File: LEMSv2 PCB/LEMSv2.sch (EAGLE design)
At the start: 18 parts, among them J2 M05, J7 FEMALE 2x3, U1 SDMMC06132, U2 DS3231

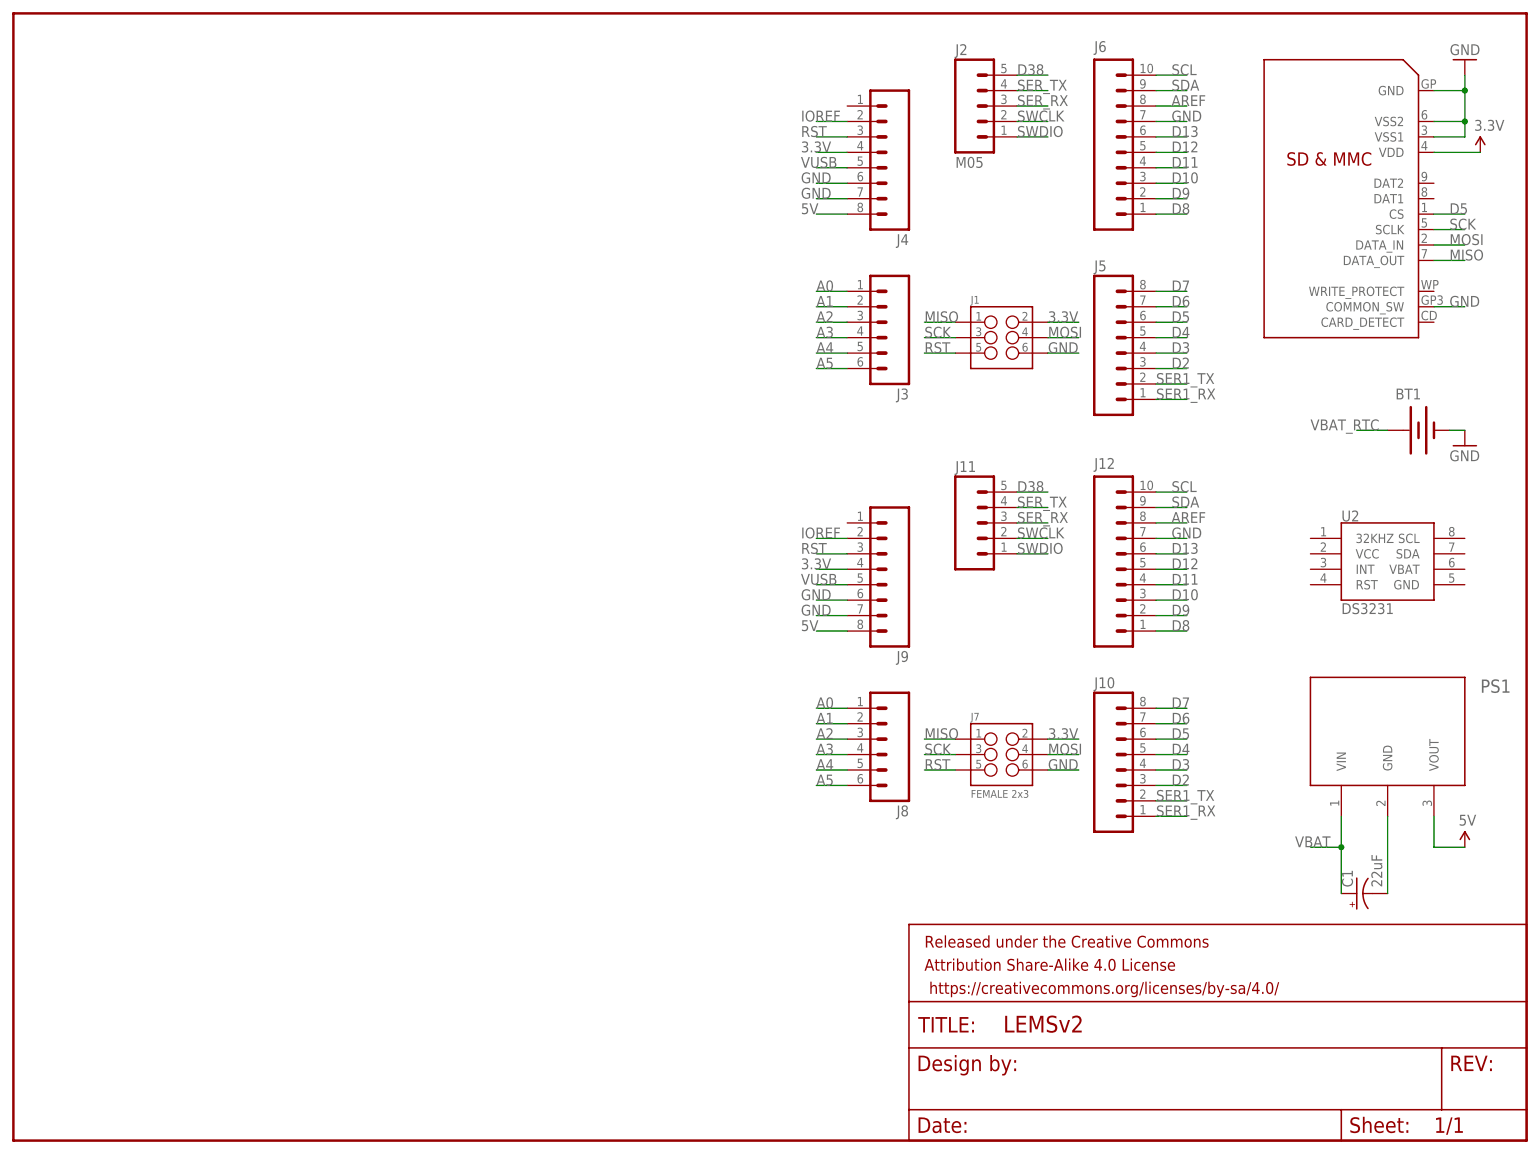
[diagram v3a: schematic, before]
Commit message: Added more parts to schematic
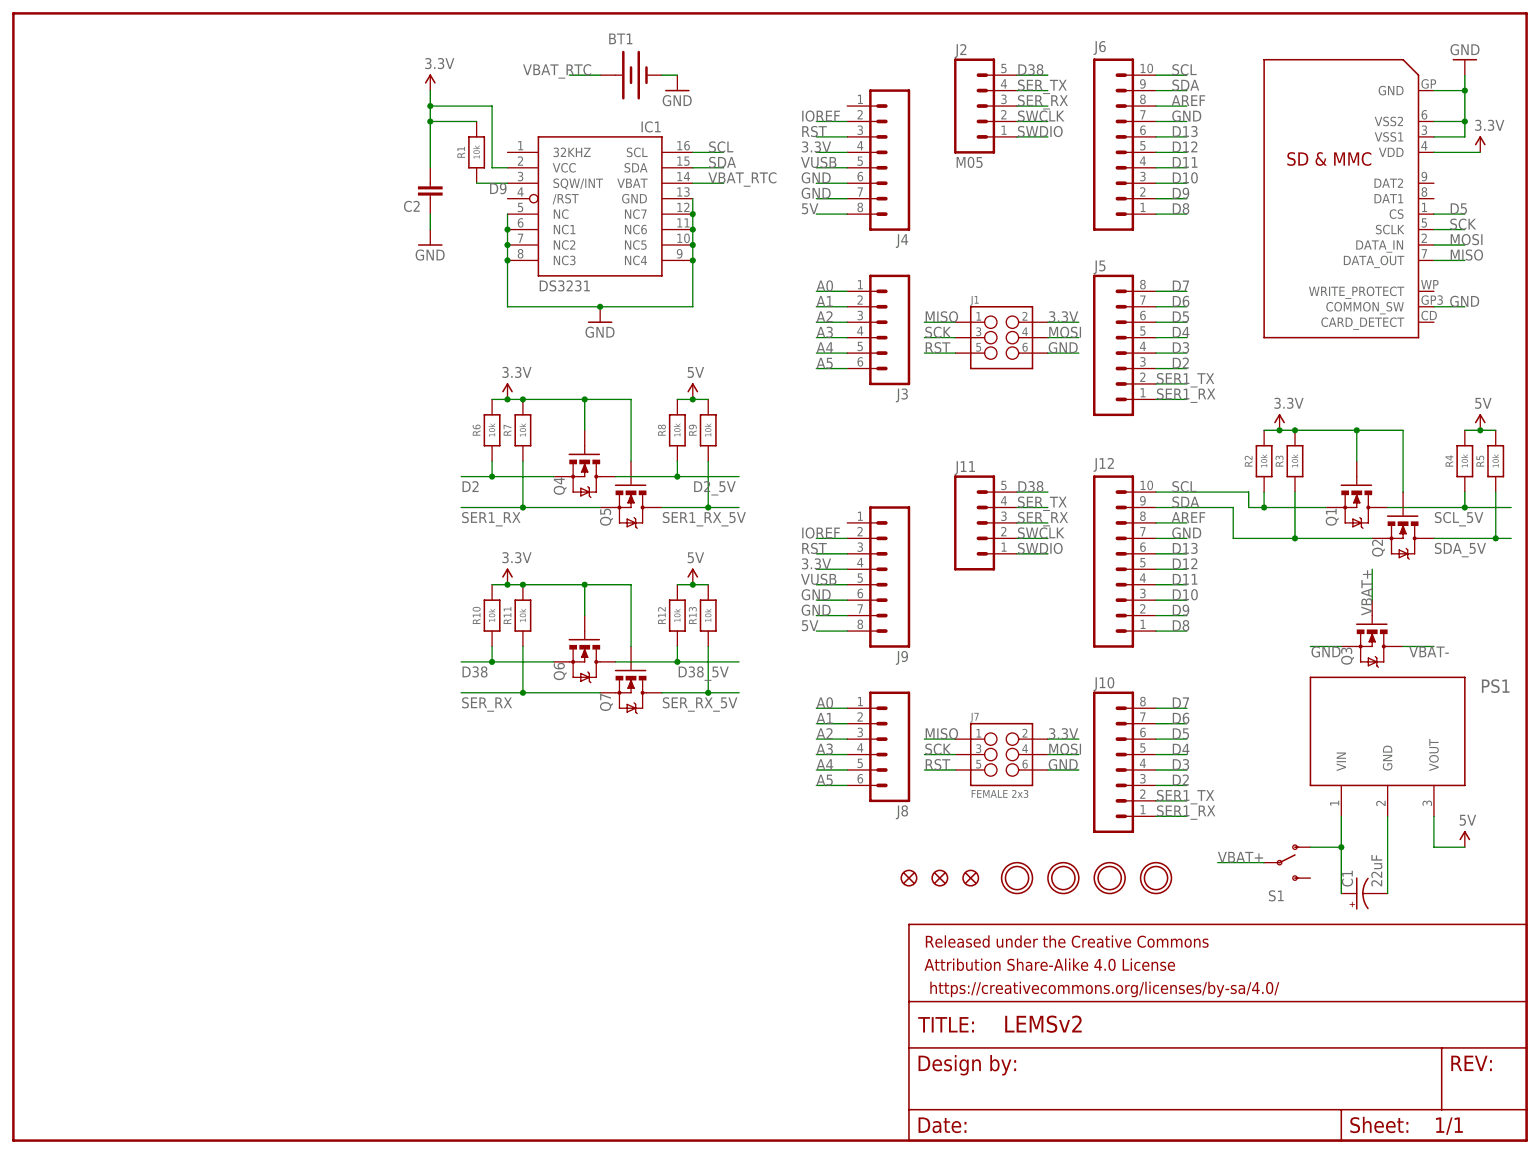
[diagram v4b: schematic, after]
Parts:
- removed U2: DS3231, LEMSv2:DS3231
- added C2: (no value), LEMSv2:CAP0805
- added FID1, FID2, FID3: FIDUCIAL"", LEMSv2:FIDUCIAL""
- added IC1: DS3231/SO, LEMSv2:DS3231/SO
- added Q1, Q2: 200mA/50V, SparkFun-DiscreteSemi:MOSFET-NCHANNELBSS138
- added Q3, Q4, Q5, Q6, Q7: 200mA/50V, LEMSv2:MOSFET-NCHANNELBSS138
- added R1, R10, R11, R12, R13, R2, R3, R4, R5, R6, R7, R8, R9: 10k, LEMSv2:RESISTOR_0805
- added S1: (no value), SparkFun-Electromechanical:SWITCH-SPDTPTH
- added U$1, U$2, U$3, U$4: MOUNTINGHOLE2.5, LEMSv2:MOUNTINGHOLE2.5
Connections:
- removed net VBAT: C1.+, PS1.VIN
- new net D2_5V: Q4.D, R8.1
- new net D38_5V: Q6.D, R12.1
- new net N$1: C1.+, PS1.VIN, S1.O
- new net SCL_5V: Q1.D, R4.1
- new net SDA_5V: Q2.D, R5.1
- new net SER1_RX_5V: Q5.D, R9.1
- new net SER_RX_5V: Q7.D, R13.1
- new net VBAT+: Q3.G, S1.P
- new net VBAT-: Q3.D
- net 3.3V: now also C2.2, IC1.VCC, Q1.G, Q2.G, Q4.G, Q5.G, Q6.G, Q7.G, R1.2, R10.2, R11.2, R2.2, R3.2, R6.2, R7.2
- net 5V: now also R12.2, R13.2, R4.2, R5.2, R8.2, R9.2
- net D2: now also Q4.S, R6.1
- net D38: now also Q6.S, R10.1
- net D9: now also IC1.SQW/INT, R1.1
- net GND: now also C2.1, IC1.GND, IC1.NC, IC1.NC1, IC1.NC2, IC1.NC3, IC1.NC4, IC1.NC5, IC1.NC6, IC1.NC7, Q3.S
- net SCL: now also IC1.SCL, Q1.S, R2.1
- net SDA: now also IC1.SDA, Q2.S, R3.1
- net SER1_RX: now also Q5.S, R7.1
- net SER_RX: now also Q7.S, R11.1
- net VBAT_RTC: now also IC1.VBAT
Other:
- moved on the sheet: BT1

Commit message: Added circuits to schematic
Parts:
- added C3: 0.1uF, LEMSv2:CAP0805
- added C4: 1uF, LEMSv2:CAP0805
- added C5, C6: (no value), LEMSv2:CAP0805
- added J13: (no value), LEMSv2:M03PTH
- added R14: (no value), adafruit:R-US_FLIPFLOP
- added U3: TLV2372, LEMSv2:TLV2372
- added U4: BMP280, LEMSv2:BMP280
- renumbered IC1 to U2
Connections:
- new net LIOUT: C4.2, R14.2, U3TLV2372-1.OUT
- new net LI_IN-: C4.1, R14.1, U3TLV2372-1.-IN
- new net N$2: J13.2, U3TLV2372-2.-IN
- new net N$3: J13.1, U3TLV2372-2.+IN
- new net N$4: J13.3, U3TLV2372-2.OUT
- net 3.3V: now also C5.1, C6.1, U4.CSB, U4.SDO, U4.VDD, U4.VDDIO
- net 5V: now also C3.1, U3TLV2372-PWRN.VCC
- net GND: now also C3.2, C5.2, C6.2, U3TLV2372-1.+IN, U3TLV2372-PWRN.GND, U4.GND@1, U4.GND@7
- net SCL: now also U4.SCK
- net SDA: now also U4.SDI

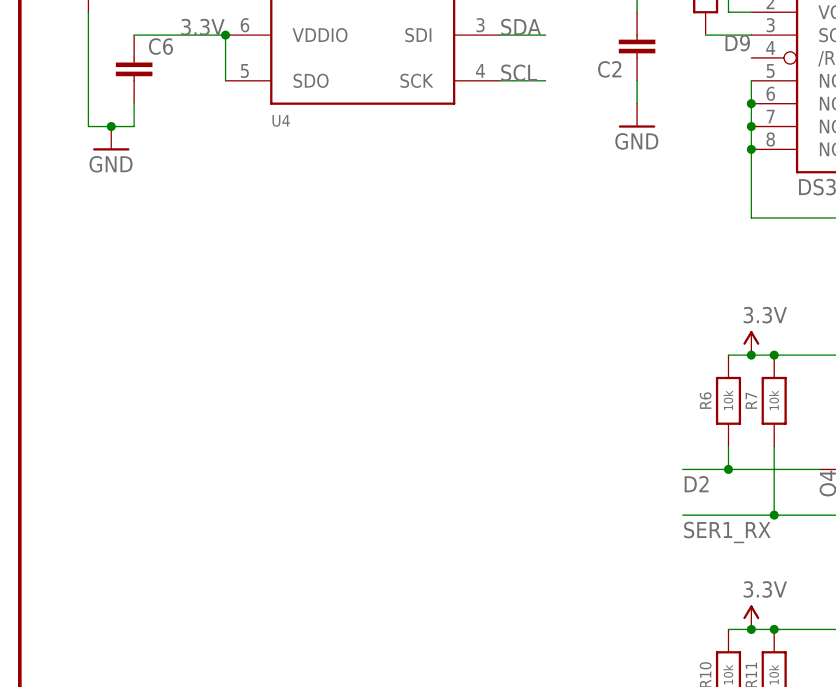
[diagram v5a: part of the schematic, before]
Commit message: Added LED circuit
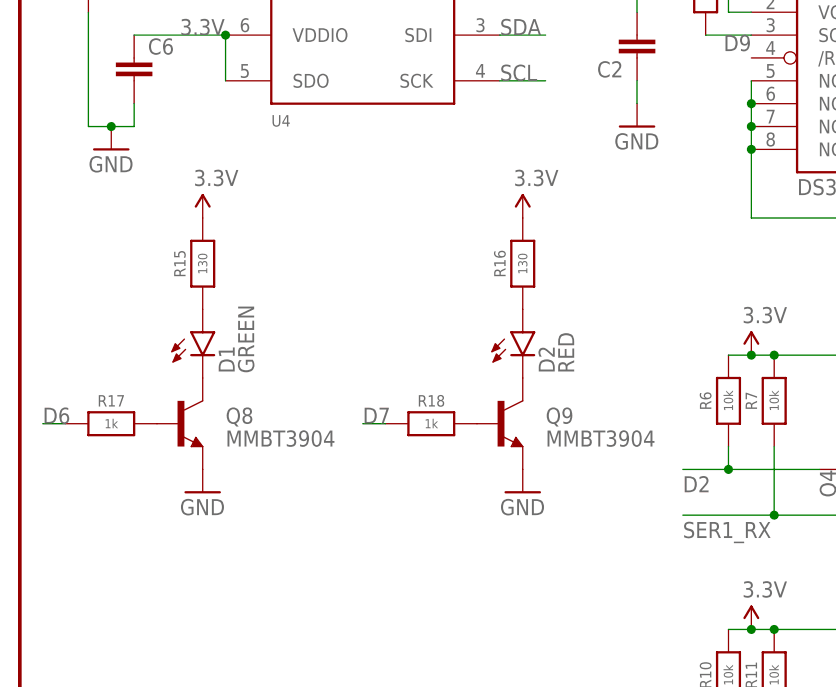
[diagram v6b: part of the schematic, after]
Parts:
- added D1: GREEN, LEMSv2:LED_GREEN
- added D2: RED, LEMSv2:LED_RED
- added Q8, Q9: MMBT3904, LEMSv2:MMBT3904
- added R15, R16: 130, LEMSv2:RESISTOR_0805
- added R17, R18: 1k, LEMSv2:RESISTOR_0805
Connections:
- new net N$10: D2.A, R16.1
- new net N$5: Q8.B, R17.2
- new net N$6: Q9.B, R18.2
- new net N$7: D1.C, Q8.C
- new net N$8: D2.C, Q9.C
- new net N$9: D1.A, R15.1
- net 3.3V: now also R15.2, R16.2
- net D6: now also R17.1
- net D7: now also R18.1
- net GND: now also Q8.E, Q9.E
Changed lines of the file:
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@@
 <part name="C6" library="LEMSv2" deviceset="CAP" device="0805"/>
 <part name="GND7" library="LEMSv2" deviceset="GND" device=""/>
+<part name="Q8" library="LEMSv2" deviceset="MMBT3904" device=""/>
+<part name="Q9" library="LEMSv2" deviceset="MMBT3904" device=""/>
+<part name="GND8" library="LEMSv2" deviceset="GND" device=""/>
+<part name="GND9" library="LEMSv2" deviceset="GND" device=""/>
+<part name="R15" library="LEMSv2" deviceset="RESISTOR" device="_0805" value="130"/>
+<part name="R16" library="LEMSv2" deviceset="RESISTOR" device="_0805" value="130"/>
+<part name="R17" library="LEMSv2" deviceset="RESISTOR" device="_0805" value="1k"/>
+<part name="R18" library="LEMSv2" deviceset="RESISTOR" device="_0805" value="1k"/>
+<part name="D1" library="LEMSv2" deviceset="LED_GREEN" device="" value="GREEN"/>
+<part name="D2" library="LEMSv2" deviceset="LED_RED" device="" value="RED"/>
+<part name="SUPPLY11" library="LEMSv2" deviceset="3.3V" device=""/>
+<part name="SUPPLY12" library="LEMSv2" deviceset="3.3V" device=""/>
 </parts>
 <sheets>
@@
 <instance part="C6" gate="G$1" x="12.7" y="152.4"/>
 <instance part="GND7" gate="1" x="10.16" y="144.78"/>
+<instance part="Q8" gate="G$1" x="17.78" y="114.3"/>
+<instance part="Q9" gate="G$1" x="53.34" y="114.3"/>
+<instance part="GND8" gate="1" x="20.32" y="106.68"/>
+<instance part="GND9" gate="1" x="55.88" y="106.68"/>
+<instance part="R15" gate="G$1" x="20.32" y="132.08" rot="R90"/>
+<instance part="R16" gate="G$1" x="55.88" y="132.08" rot="R90"/>
+<instance part="R17" gate="G$1" x="10.16" y="114.3"/>
+<instance part="R18" gate="G$1" x="45.72" y="114.3"/>
+<instance part="D1" gate="G$1" x="20.32" y="124.46"/>
+<instance part="D2" gate="G$1" x="55.88" y="124.46"/>
+<instance part="SUPPLY11" gate="G$1" x="20.32" y="137.16"/>
+<instance part="SUPPLY12" gate="G$1" x="55.88" y="137.16"/>
 </instances>
 <busses>
@@
 <wire x1="53.34" y1="162.56" x2="58.42" y2="162.56" width="0.1524" layer="91"/>
 <label x="53.34" y="162.56" size="1.778" layer="95"/>
+</segment>
+<segment>
+<pinref part="R15" gate="G$1" pin="2"/>
+<pinref part="SUPPLY11" gate="G$1" pin="3.3V"/>
+</segment>
+<segment>
+<pinref part="R16" gate="G$1" pin="2"/>
+<pinref part="SUPPLY12" gate="G$1" pin="3.3V"/>
 </segment>
 </net>
@@
 <junction x="10.16" y="147.32"/>
 </segment>
+<segment>
+<pinref part="Q8" gate="G$1" pin="E"/>
+<pinref part="GND8" gate="1" pin="GND"/>
+</segment>
+<segment>
+<pinref part="Q9" gate="G$1" pin="E"/>
+<pinref part="GND9" gate="1" pin="GND"/>
+</segment>
 </net>
 <net name="SCK" class="0">
@@
 <label x="190.5" y="71.12" size="1.778" layer="95"/>
 </segment>
+<segment>
+<pinref part="R18" gate="G$1" pin="1"/>
+<wire x1="40.64" y1="114.3" x2="38.1" y2="114.3" width="0.1524" layer="91"/>
+<label x="38.1" y="114.3" size="1.778" layer="95"/>
+</segment>
 </net>
 <net name="D6" class="0">
@@
 <wire x1="187.96" y1="68.58" x2="193.04" y2="68.58" width="0.1524" layer="91"/>
 <label x="190.5" y="68.58" size="1.778" layer="95"/>
+</segment>
+<segment>
+<pinref part="R17" gate="G$1" pin="1"/>
+<wire x1="5.08" y1="114.3" x2="2.54" y2="114.3" width="0.1524" layer="91"/>
+<label x="2.54" y="114.3" size="1.778" layer="95"/>
 </segment>
 </net>
@@
 </segment>
 </net>
+<net name="N$5" class="0">
+<segment>
+<pinref part="Q8" gate="G$1" pin="B"/>
+<pinref part="R17" gate="G$1" pin="2"/>
+</segment>
+</net>
+<net name="N$6" class="0">
+<segment>
+<pinref part="Q9" gate="G$1" pin="B"/>
+<pinref part="R18" gate="G$1" pin="2"/>
+</segment>
+</net>
+<net name="N$7" class="0">
+<segment>
+<pinref part="Q8" gate="G$1" pin="C"/>
+<pinref part="D1" gate="G$1" pin="C"/>
+</segment>
+</net>
+<net name="N$8" class="0">
+<segment>
+<pinref part="Q9" gate="G$1" pin="C"/>
+<pinref part="D2" gate="G$1" pin="C"/>
+</segment>
+</net>
+<net name="N$9" class="0">
+<segment>
+<pinref part="D1" gate="G$1" pin="A"/>
+<pinref part="R15" gate="G$1" pin="1"/>
+</segment>
+</net>
+<net name="N$10" class="0">
+<segment>
+<pinref part="D2" gate="G$1" pin="A"/>
+<pinref part="R16" gate="G$1" pin="1"/>
+</segment>
+</net>
